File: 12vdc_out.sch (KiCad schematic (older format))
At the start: 3 parts, among them U1 LM7812

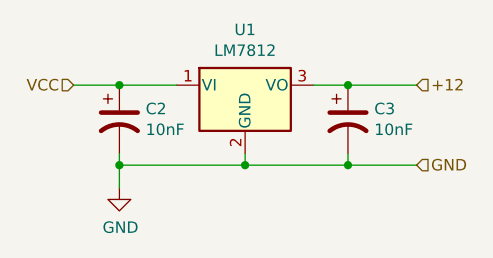
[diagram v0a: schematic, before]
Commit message: Fixed ERC errors, combined all outputs into a bus, fixed annotations
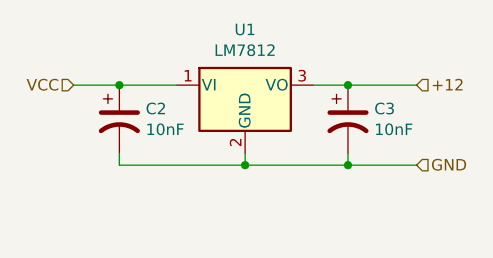
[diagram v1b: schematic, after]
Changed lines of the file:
@@
 Wire Wire Line
 	5800 2050 6100 2050
-$Comp
-L power:GND #PWR0103
-U 1 1 5E70EA56
-P 4800 2500
-F 0 "#PWR0103" H 4800 2250 50  0001 C CNN
-F 1 "GND" H 4805 2327 50  0000 C CNN
-F 2 "" H 4800 2500 50  0001 C CNN
-F 3 "" H 4800 2500 50  0001 C CNN
-	1    4800 2500
-	1    0    0    -1
-$EndComp
-Wire Wire Line
-	4800 2400 4800 2500
-Connection ~ 4800 2400
 $EndSCHEMATC
